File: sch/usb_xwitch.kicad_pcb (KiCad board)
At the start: 2 copper layers, 65 x 56.5 mm, 63 parts, among them J1 USB3_A, J2 USB3_A, J3 USB3_A, J4 USB3_A, J5 USB3_A, J6 USB3_A, J7 USB3_A, J8 Conn_02x05_Odd_Even, J9 C65114, K1 Relay_DPDT_Panasonic_AGQ200A4H, K2 Relay_DPDT_Panasonic_AGQ200A4H, K3 Relay_DPDT_Panasonic_AGQ200A4H, Q1 2N7002P, Q2 2N7002P, Q3 2N7002P, SW1 C2689642, U1 Pico

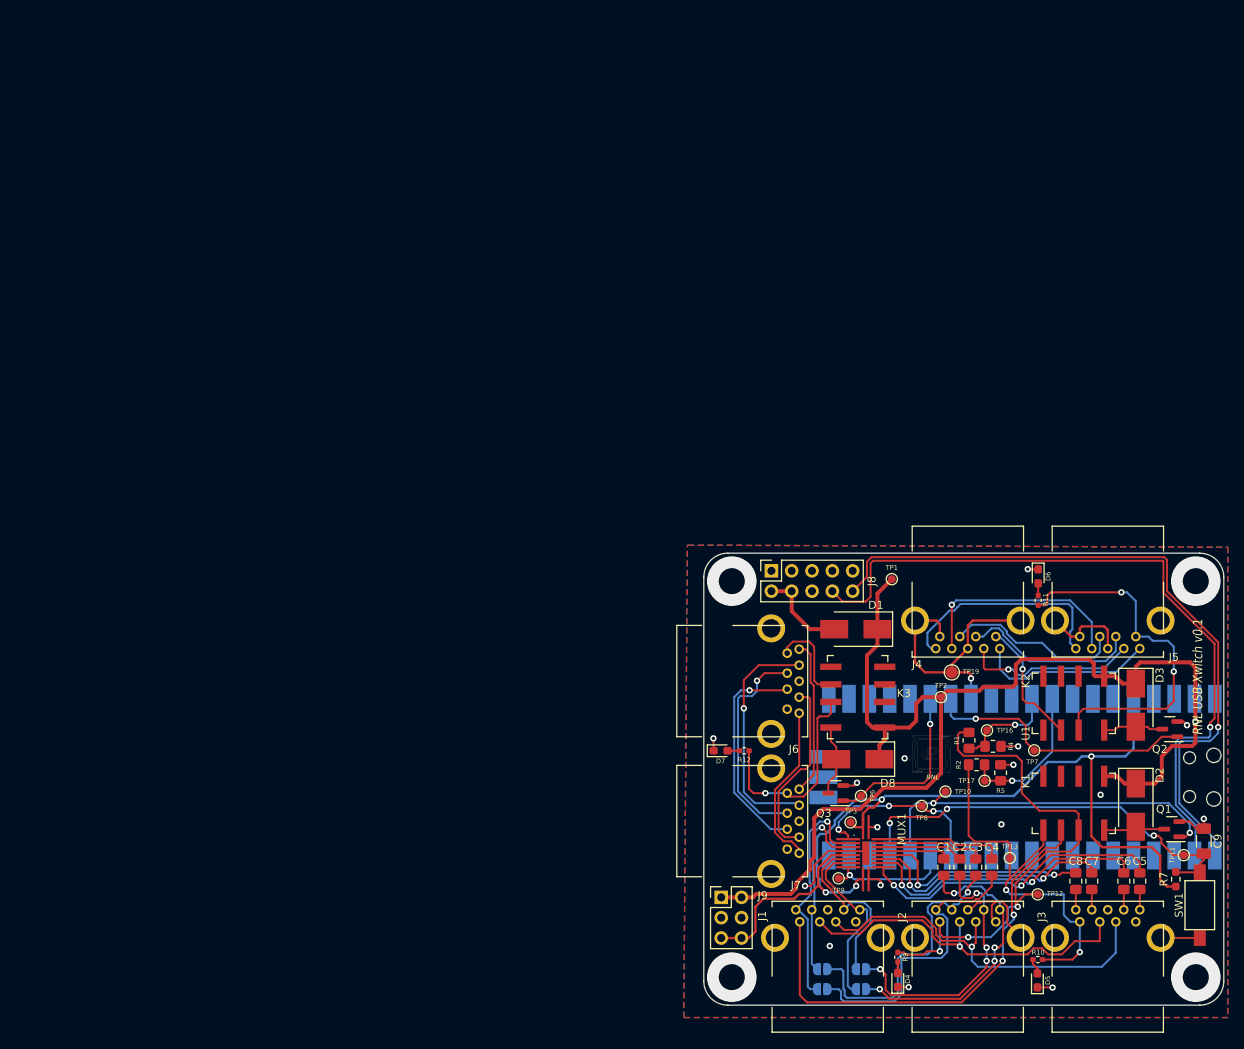
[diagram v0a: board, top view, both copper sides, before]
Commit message: updated 3d models, broken footprints, pcb re-import
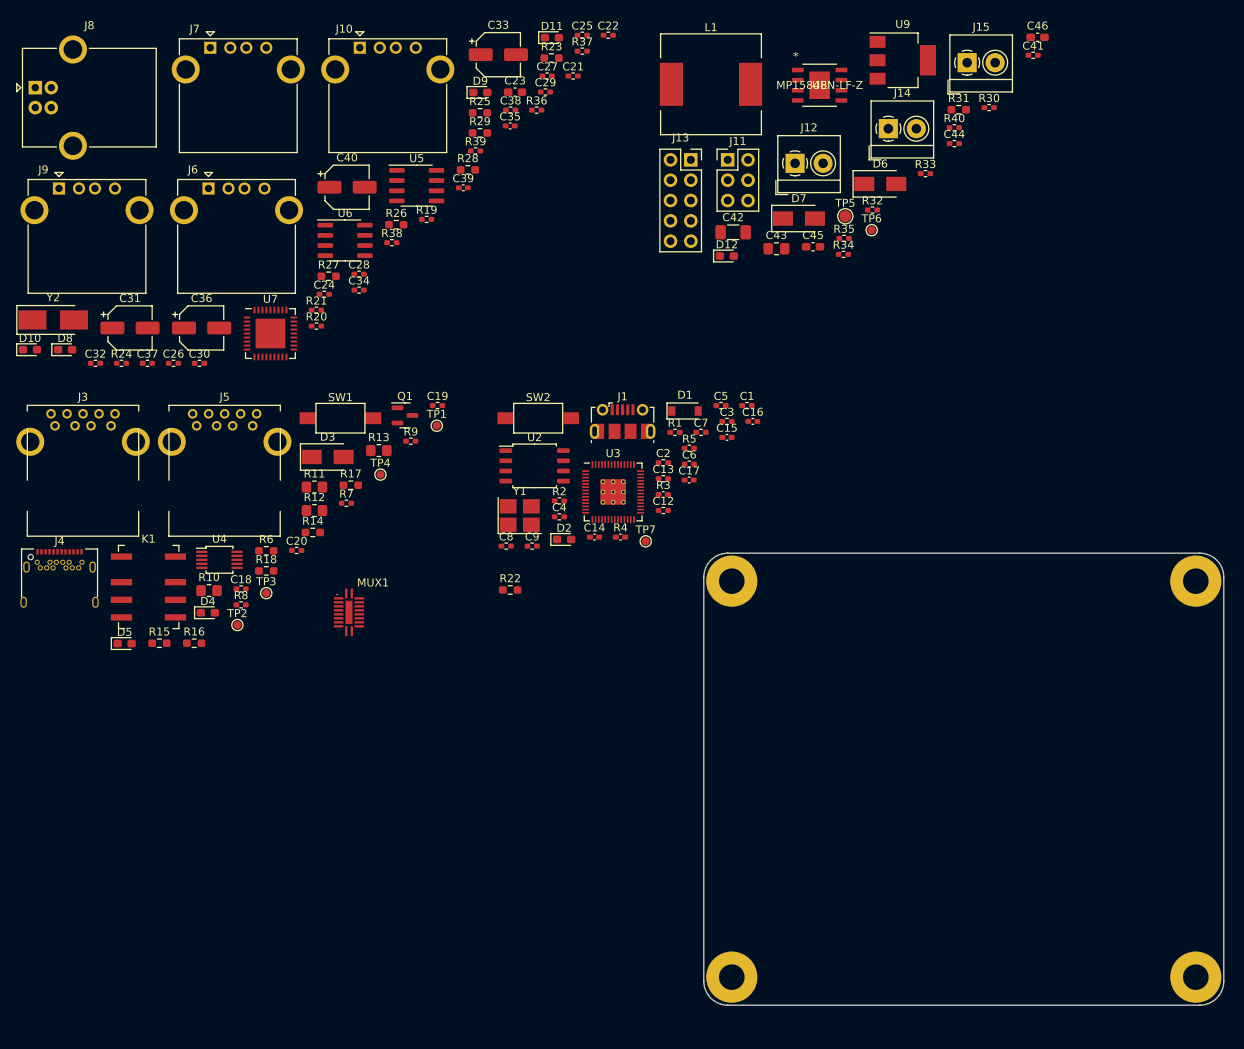
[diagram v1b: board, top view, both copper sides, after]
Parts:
- removed J2: USB3_A, usb_xwitch:USB3_A_AdamTech_USB-A3-S-RA
- removed JP1, JP2, JP3, JP4: SolderJumper_2_Open, Jumper:SolderJumper-2_P1.3mm_Open_RoundedPad1.0x1.5mm
- removed K2, K3: Relay_DPDT_Panasonic_AGQ200A4H, usb_xwitch:Relay_DPDT_Panasonic_AGQ200A4H
- removed Q2, Q3: 2N7002P, Package_TO_SOT_SMD:SOT-23
- removed RNL: LOGO, LOGO
- removed TP10, TP11, TP12, TP13, TP16, TP17, TP8, TP9: TestPoint, TestPoint:TestPoint_Pad_D1.0mm
- removed TP19: TestPoint, TestPoint:TestPoint_Pad_D1.5mm
- removed U1: Pico, usb_xwitch:RPi_Pico_SMD
- added C12: 1u, Resistor_SMD:R_0402_1005Metric_Pad0.72x0.64mm_HandSolder, F.Cu at (94.9, 74.7)
- added C13: 1u, Resistor_SMD:R_0402_1005Metric_Pad0.72x0.64mm_HandSolder, F.Cu at (94.9, 70.7)
- added C14: 2.2u, Inductor_SMD:L_0402_1005Metric_Pad0.77x0.64mm_HandSolder, F.Cu at (86.3, 78.0)
- added C15: 100n, Inductor_SMD:L_0402_1005Metric_Pad0.77x0.64mm_HandSolder, F.Cu at (102.9, 65.5)
- added C16: 30pF, Capacitor_SMD:C_0402_1005Metric_Pad0.74x0.62mm_HandSolder, F.Cu at (106.1, 63.5)
- added C17: 30pF, Capacitor_SMD:C_0402_1005Metric_Pad0.74x0.62mm_HandSolder, F.Cu at (98.2, 70.9)
- added C18: 100n, Resistor_SMD:R_0402_1005Metric_Pad0.72x0.64mm_HandSolder, F.Cu at (42.2, 84.5)
- added C19: 100n, Resistor_SMD:R_0402_1005Metric_Pad0.72x0.64mm_HandSolder, F.Cu at (66.7, 61.5)
- added C20: 100n, Resistor_SMD:R_0402_1005Metric_Pad0.72x0.64mm_HandSolder, F.Cu at (49.1, 79.7)
- added C21: 100n, Resistor_SMD:R_0402_1005Metric_Pad0.72x0.64mm_HandSolder, F.Cu at (83.7, 20.4)
- added C22: 100n, Resistor_SMD:R_0402_1005Metric_Pad0.72x0.64mm_HandSolder, F.Cu at (88.1, 15.3)
- added C23: 4.7u, Capacitor_SMD:C_0603_1608Metric_Pad1.08x0.95mm_HandSolder, F.Cu at (76.4, 22.4)
- added C24: 100n, Resistor_SMD:R_0402_1005Metric_Pad0.72x0.64mm_HandSolder, F.Cu at (52.6, 47.6)
- added C25: 100n, Resistor_SMD:R_0402_1005Metric_Pad0.72x0.64mm_HandSolder, F.Cu at (84.8, 15.3)
- added C26: 1u, Resistor_SMD:R_0402_1005Metric_Pad0.72x0.64mm_HandSolder, F.Cu at (33.7, 56.3)
- added C27: 100n, Resistor_SMD:R_0402_1005Metric_Pad0.72x0.64mm_HandSolder, F.Cu at (80.4, 20.4)
- added C28: 100n, Resistor_SMD:R_0402_1005Metric_Pad0.72x0.64mm_HandSolder, F.Cu at (56.9, 45.1)
- added C29: 100n, Resistor_SMD:R_0402_1005Metric_Pad0.72x0.64mm_HandSolder, F.Cu at (80.2, 22.4)
- added C30: 100n, Resistor_SMD:R_0402_1005Metric_Pad0.72x0.64mm_HandSolder, F.Cu at (37.0, 56.3)
- added C31: 100u, Capacitor_SMD:CP_Elec_5x5.4, F.Cu at (28.3, 51.9)
- added C32: 1u, Resistor_SMD:R_0402_1005Metric_Pad0.72x0.64mm_HandSolder, F.Cu at (24.0, 56.3)
- added C33: 100u, Capacitor_SMD:CP_Elec_5x5.4, F.Cu at (74.3, 17.7)
- added C34: 100n, Resistor_SMD:R_0402_1005Metric_Pad0.72x0.64mm_HandSolder, F.Cu at (56.9, 47.1)
- added C35: 27p, Capacitor_SMD:C_0402_1005Metric_Pad0.74x0.62mm_HandSolder, F.Cu at (75.8, 26.6)
- added C36: 100u, Capacitor_SMD:CP_Elec_5x5.4, F.Cu at (37.2, 51.9)
- added C37: 100n, Resistor_SMD:R_0402_1005Metric_Pad0.72x0.64mm_HandSolder, F.Cu at (30.5, 56.3)
- added C38: 100n, Resistor_SMD:R_0402_1005Metric_Pad0.72x0.64mm_HandSolder, F.Cu at (75.9, 24.6)
- added C39: 27p, Capacitor_SMD:C_0402_1005Metric_Pad0.74x0.62mm_HandSolder, F.Cu at (69.9, 34.3)
- added C40: 100u, Capacitor_SMD:CP_Elec_5x5.4, F.Cu at (55.4, 34.3)
- added C41: 100n, Resistor_SMD:R_0402_1005Metric_Pad0.72x0.64mm_HandSolder, F.Cu at (141.2, 17.8)
- added C42: 22u, Capacitor_SMD:C_1206_3216Metric_Pad1.33x1.80mm_HandSolder, F.Cu at (103.7, 39.9)
- added C43: 10u, Capacitor_SMD:C_0805_2012Metric_Pad1.18x1.45mm_HandSolder, F.Cu at (109.1, 42.0)
- added C44: 150pF, Resistor_SMD:R_0402_1005Metric_Pad0.72x0.64mm_HandSolder, F.Cu at (131.3, 28.8)
- added C45: 10u, Capacitor_SMD:C_0603_1608Metric_Pad1.08x0.95mm_HandSolder, F.Cu at (113.7, 41.7)
- added C46: 10u, Capacitor_SMD:C_0603_1608Metric_Pad1.08x0.95mm_HandSolder, F.Cu at (141.7, 15.5)
- added D10: 19-217/GHC-YR1S2/3T, Diode_SMD:D_0603_1608Metric_Pad1.05x0.95mm_HandSolder, F.Cu at (15.8, 54.6)
- added D11: 19-217/GHC-YR1S2/3T, Diode_SMD:D_0603_1608Metric_Pad1.05x0.95mm_HandSolder, F.Cu at (81.0, 15.6)
- added D12: 19-217/GHC-YR1S2/3T, Diode_SMD:D_0603_1608Metric_Pad1.05x0.95mm_HandSolder, F.Cu at (102.9, 42.9)
- added D9: 19-217/GHC-YR1S2/3T, Diode_SMD:D_0603_1608Metric_Pad1.05x0.95mm_HandSolder, F.Cu at (72.1, 22.4)
- added H1: RPI Mounting Hole, MountingHole:MountingHole_3.2mm_M3_Pad, F.Cu at (103.5, 83.5)
- added H2: RPI Mounting Hole, MountingHole:MountingHole_3.2mm_M3_Pad, F.Cu at (161.5, 83.5)
- added H3: RPI Mounting Hole, MountingHole:MountingHole_3.2mm_M3_Pad, F.Cu at (161.5, 133.0)
- added H4: RPI Mounting Hole, MountingHole:MountingHole_3.2mm_M3_Pad, F.Cu at (103.5, 133.0)
- added J10: USB_A, Connector_USB:USB_A_CONNFLY_DS1095-WNR0, F.Cu at (57.0, 16.8)
- added J11: C65114, Connector_PinHeader_2.54mm:PinHeader_2x03_P2.54mm_Vertical, F.Cu at (103.0, 30.8)
- added J12: Screw_Terminal_3.5mm, TerminalBlock_4Ucon:TerminalBlock_4Ucon_1x02_P3.50mm_Horizontal, F.Cu at (111.4, 31.3)
- added J13: Conn_02x05_Odd_Even, Connector_PinSocket_2.54mm:PinSocket_2x05_P2.54mm_Vertical, F.Cu at (98.4, 30.8)
- added J14: Screw_Terminal_3.5mm, TerminalBlock_4Ucon:TerminalBlock_4Ucon_1x02_P3.50mm_Horizontal, F.Cu at (123.1, 26.9)
- added J15: Screw_Terminal_3.5mm, TerminalBlock_4Ucon:TerminalBlock_4Ucon_1x02_P3.50mm_Horizontal, F.Cu at (132.9, 18.7)
- added L1: 15u, Inductor_SMD:L_12x12mm_H6mm, F.Cu at (100.9, 21.4)
- added R13: 33K, Resistor_SMD:R_0805_2012Metric_Pad1.20x1.40mm_HandSolder, F.Cu at (59.4, 67.2)
- added R14: 0R, Resistor_SMD:R_0603_1608Metric_Pad0.98x0.95mm_HandSolder, F.Cu at (51.1, 77.4)
- added R15: 0R, Resistor_SMD:R_0603_1608Metric_Pad0.98x0.95mm_HandSolder, F.Cu at (31.9, 91.3)
- added R16: 0R, Resistor_SMD:R_0603_1608Metric_Pad0.98x0.95mm_HandSolder, F.Cu at (36.3, 91.3)
- added R17: 0R, Resistor_SMD:R_0603_1608Metric_Pad0.98x0.95mm_HandSolder, F.Cu at (55.9, 71.5)
- added R18: 0R, Resistor_SMD:R_0603_1608Metric_Pad0.98x0.95mm_HandSolder, F.Cu at (45.3, 82.2)
- added R19: 100K, Resistor_SMD:R_0402_1005Metric_Pad0.72x0.64mm_HandSolder, F.Cu at (65.4, 38.3)
- added R20: 100K, Resistor_SMD:R_0402_1005Metric_Pad0.72x0.64mm_HandSolder, F.Cu at (51.6, 51.6)
- added R21: 100K, Resistor_SMD:R_0402_1005Metric_Pad0.72x0.64mm_HandSolder, F.Cu at (51.6, 49.6)
- added R22: 12K, Resistor_SMD:R_0603_1608Metric_Pad0.98x0.95mm_HandSolder, F.Cu at (75.8, 84.6)
- added R23: 1M, Resistor_SMD:R_0603_1608Metric_Pad0.98x0.95mm_HandSolder, F.Cu at (81.0, 18.1)
- added R24: 100K, Resistor_SMD:R_0402_1005Metric_Pad0.72x0.64mm_HandSolder, F.Cu at (27.2, 56.3)
- added R25: 10K, Resistor_SMD:R_0603_1608Metric_Pad0.98x0.95mm_HandSolder, F.Cu at (72.0, 25.0)
- added R26: 10K, Resistor_SMD:R_0603_1608Metric_Pad0.98x0.95mm_HandSolder, F.Cu at (61.6, 38.9)
- added R27: 100K, Resistor_SMD:R_0603_1608Metric_Pad0.98x0.95mm_HandSolder, F.Cu at (53.1, 45.4)
- added R28: 100K, Resistor_SMD:R_0603_1608Metric_Pad0.98x0.95mm_HandSolder, F.Cu at (70.5, 32.1)
- added R29: 10K, Resistor_SMD:R_0603_1608Metric_Pad0.98x0.95mm_HandSolder, F.Cu at (72.0, 27.5)
- added R3: 1K, Inductor_SMD:L_0402_1005Metric_Pad0.77x0.64mm_HandSolder, F.Cu at (94.9, 72.7)
- added R30: 100K, Resistor_SMD:R_0402_1005Metric_Pad0.72x0.64mm_HandSolder, F.Cu at (135.7, 24.3)
- added R31: 24.9k, Resistor_SMD:R_0603_1608Metric_Pad0.98x0.95mm_HandSolder, F.Cu at (131.9, 24.6)
- added R32: 210k, Resistor_SMD:R_0402_1005Metric_Pad0.72x0.64mm_HandSolder, F.Cu at (121.1, 37.1)
- added R33: 100K, Resistor_SMD:R_0402_1005Metric_Pad0.72x0.64mm_HandSolder, F.Cu at (127.7, 32.6)
- added R34: 40.2K, Resistor_SMD:R_0402_1005Metric_Pad0.72x0.64mm_HandSolder, F.Cu at (117.5, 42.6)
- added R35: 100K, Resistor_SMD:R_0402_1005Metric_Pad0.72x0.64mm_HandSolder, F.Cu at (117.5, 40.7)
- added R36: 330, Resistor_SMD:R_0402_1005Metric_Pad0.72x0.64mm_HandSolder, F.Cu at (79.1, 24.6)
- added R37: 330, Resistor_SMD:R_0402_1005Metric_Pad0.72x0.64mm_HandSolder, F.Cu at (84.8, 17.2)
- added R38: 330, Resistor_SMD:R_0402_1005Metric_Pad0.72x0.64mm_HandSolder, F.Cu at (61.0, 41.2)
- added R39: 330, Resistor_SMD:R_0402_1005Metric_Pad0.72x0.64mm_HandSolder, F.Cu at (71.5, 29.7)
- added R40: 510, Resistor_SMD:R_0402_1005Metric_Pad0.72x0.64mm_HandSolder, F.Cu at (131.3, 26.8)
- added R6: 10K, Resistor_SMD:R_0603_1608Metric_Pad0.98x0.95mm_HandSolder, F.Cu at (45.3, 79.7)
- added R8: 330, Resistor_SMD:R_0402_1005Metric_Pad0.72x0.64mm_HandSolder, F.Cu at (42.2, 86.5)
- added SW2: C2689642, usb_xwitch:SW_SPST_CK_PTS636_SP43_SMTR, F.Cu at (79.3, 63.1)
- added TP4: TestPoint, TestPoint:TestPoint_Pad_D1.0mm, F.Cu at (59.6, 70.2)
- added TP5: TestPoint, TestPoint:TestPoint_Pad_D1.5mm, F.Cu at (117.7, 37.9)
- added U2: W25Q64JVSSIQ, Package_SO:SOIC-8_5.23x5.23mm_P1.27mm, F.Cu at (78.8, 69.1)
- added U3: RP2040, usb_xwitch:RP2040-QFN-56, F.Cu at (88.7, 72.3)
- added U4: FSUSB42MUX, Package_SO:MSOP-10_3x3mm_P0.5mm, F.Cu at (39.5, 80.8)
- added U5: MIC2026-1BM, Package_SO:SOIC-8_3.9x4.9mm_P1.27mm, F.Cu at (64.1, 34.1)
- added U6: MIC2026-1BM, Package_SO:SOIC-8_3.9x4.9mm_P1.27mm, F.Cu at (55.2, 40.9)
- added U7: USB2514B_Bi, Package_DFN_QFN:QFN-36-1EP_6x6mm_P0.5mm_EP3.7x3.7mm, F.Cu at (45.8, 52.5)
- added U8: MP1584EN-LF-Z, usb_xwitch:MP1584EN-LF-Z, F.Cu at (114.5, 21.5)
- added U9: NCP1117LPST33T3G, Package_TO_SOT_SMD:SOT-223-3_TabPin2, F.Cu at (124.9, 18.4)
- added Y1: 12MHz, Crystal:Crystal_SMD_3225-4Pin_3.2x2.5mm_HandSoldering, F.Cu at (77.0, 75.3)
- added Y2: 24MHz, Crystal:Crystal_SMD_5032-2Pin_5.0x3.2mm_HandSoldering, F.Cu at (18.7, 50.9)
- C1, C2, C3, C4, C5, C6, C7, C8: footprint Capacitor_SMD:C_0805_2012Metric_Pad1.18x1.45mm_HandSolder -> Resistor_SMD:R_0402_1005Metric_Pad0.72x0.64mm_HandSolder
- C9: footprint Capacitor_SMD:C_1206_3216Metric_Pad1.33x1.80mm_HandSolder -> Resistor_SMD:R_0402_1005Metric_Pad0.72x0.64mm_HandSolder
- D1: value VS-10BQ015 -> B5819W SL; footprint Diode_SMD:D_SMB_Handsoldering -> Diode_SMD:D_SOD-123
- D2, D8: value VS-10BQ015 -> 19-217/GHC-YR1S2/3T; footprint Diode_SMD:D_SMB_Handsoldering -> Diode_SMD:D_0603_1608Metric_Pad1.05x0.95mm_HandSolder
- D3: value VS-10BQ015 -> SS34; footprint Diode_SMD:D_SMB_Handsoldering -> Diode_SMD:D_SMA
- D6, D7: value 19-217/GHC-YR1S2/3T -> SS34; footprint Diode_SMD:D_0603_1608Metric_Pad1.05x0.95mm_HandSolder -> Diode_SMD:D_SMA
- J1: value USB3_A -> USB_B_Micro; footprint usb_xwitch:USB3_A_AdamTech_USB-A3-S-RA -> Connector_USB:USB_Micro-B_Molex-105017-0001
- J4: value USB3_A -> USB_C_Receptacle; footprint usb_xwitch:USB3_A_AdamTech_USB-A3-S-RA -> usb_xwitch:USB_TypeC_24Pin_ShouHan
- J6, J7: value USB3_A -> USB_A; footprint usb_xwitch:USB3_A_AdamTech_USB-A3-S-RA -> Connector_USB:USB_A_CONNFLY_DS1095-WNR0
- J8: value Conn_02x05_Odd_Even -> USB_B; footprint Connector_PinSocket_2.54mm:PinSocket_2x05_P2.54mm_Vertical -> Connector_USB:USB_B_OST_USB-B1HSxx_Horizontal
- J9: value C65114 -> USB_A; footprint Connector_PinHeader_2.54mm:PinHeader_2x03_P2.54mm_Vertical -> Connector_USB:USB_A_CONNFLY_DS1095-WNR0
- R1, R2: value 18K -> 27.4R; footprint Resistor_SMD:R_0805_2012Metric_Pad1.20x1.40mm_HandSolder -> Resistor_SMD:R_0402_1005Metric_Pad0.72x0.64mm_HandSolder
- R10, R11: value 330Ω -> 18K; footprint Resistor_SMD:R_0402_1005Metric_Pad0.72x0.64mm_HandSolder -> Resistor_SMD:R_0805_2012Metric_Pad1.20x1.40mm_HandSolder
- R12: value 330Ω -> 33K; footprint Resistor_SMD:R_0402_1005Metric_Pad0.72x0.64mm_HandSolder -> Resistor_SMD:R_0805_2012Metric_Pad1.20x1.40mm_HandSolder
- R4: value 33K -> 1K; footprint Resistor_SMD:R_0805_2012Metric_Pad1.20x1.40mm_HandSolder -> Inductor_SMD:L_0402_1005Metric_Pad0.77x0.64mm_HandSolder
- R5: value 33K -> 470R; footprint Resistor_SMD:R_0805_2012Metric_Pad1.20x1.40mm_HandSolder -> Resistor_SMD:R_0402_1005Metric_Pad0.72x0.64mm_HandSolder
- R7: value 10K -> 330; footprint Resistor_SMD:R_0603_1608Metric_Pad0.98x0.95mm_HandSolder -> Resistor_SMD:R_0402_1005Metric_Pad0.72x0.64mm_HandSolder
- R9: value 330Ω -> 56K
- moved J3 142.3 mm to (18.9, 64.1)
- moved SW1 123.5 mm to (54.6, 63.1), turned to 0 degrees
- moved D5 121.6 mm to (27.6, 91.3), turned to 0 degrees
- moved J9 121.3 mm to (19.4, 34.4)
- moved J5 120.3 mm to (36.6, 64.1), turned to 0 degrees
- moved K1 118.8 mm to (30.6, 84.2), turned to 0 degrees
- moved J7 117.8 mm to (38.3, 16.8), turned to 0 degrees
- moved J4 117.2 mm to (19.5, 84.8), turned to 0 degrees
- moved R7 113.8 mm to (55.3, 73.8), turned to 0 degrees
- moved R10 113.4 mm to (38.2, 84.7), turned to 0 degrees
- moved D8 111.5 mm to (20.2, 54.6), turned to 0 degrees
- moved J8 110.1 mm to (16.4, 21.8), turned to 0 degrees
- moved Q1 108.9 mm to (62.6, 62.8), turned to 0 degrees
- moved D3 105.7 mm to (53.0, 68.0), turned to 0 degrees
- moved D4 97.7 mm to (38.0, 87.5), turned to 0 degrees
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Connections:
- C1 pad 1: Net-(C1-Pad1) -> +1V1
- C1 pad 2: /RX-BP1 -> GND
- C2 pad 1: Net-(C2-Pad1) -> +1V1
- C2 pad 2: /RX+BP1 -> GND
- C3 pad 1: Net-(C3-Pad1) -> +3V3
- C3 pad 2: /TX-BP1 -> GND
- C4 pad 1: Net-(C4-Pad1) -> +3V3
- C4 pad 2: /TX+BP1 -> GND
- C5 pad 1: Net-(C5-Pad1) -> +3V3
- C5 pad 2: Net-(C5-Pad2) -> GND
- C6 pad 1: Net-(C6-Pad1) -> +3V3
- C6 pad 2: Net-(C6-Pad2) -> GND
- C7 pad 1: Net-(C7-Pad1) -> +3V3
- C7 pad 2: Net-(C7-Pad2) -> GND
- C8 pad 1: Net-(C8-Pad1) -> +3V3
- C8 pad 2: Net-(C8-Pad2) -> GND
- C9 pad 1: GND -> +3V3
- C9 pad 2: /SW-A -> GND
- D2 pad 1: +5V -> GND
- D2 pad 2: /RL1 -> Net-(D2-Pad2)
- D3 pad 2: /RL2 -> /usb3_switch/RL1
- D6 pad 1: GND -> Net-(C41-Pad1)
- D6 pad 2: Net-(D6-Pad2) -> GND
- D7 pad 1: GND -> +5V
- D8 pad 1: +5V -> GND
- D8 pad 2: /RL3 -> Net-(D8-Pad2)
- J1 pad 1: Net-(J1-Pad1) -> Net-(D1-Pad2)
- J1 pad 2: Net-(J1-Pad2) -> /xwitch_controller/USB_D-
- J1 pad 3: Net-(J1-Pad3) -> /xwitch_controller/USB_D+
- J1 pad 4: GND -> unconnected-(J1-Pad4)
- J1 pad 5: /RX-BP -> GND
- J1 pad 6: /RX+BP -> GND
- J3 pad 1: /VBUS_1_2 -> /usb3_switch/VBUS_1_1
- J3 pad 10: GND -> Net-(J3-Pad10)
- J3 pad 2: Net-(J1-Pad2) -> Net-(J3-Pad2)
- J3 pad 3: Net-(J1-Pad3) -> Net-(J3-Pad3)
- J3 pad 4: GND -> Net-(J3-Pad4)
- J3 pad 5: Net-(C5-Pad2) -> Net-(J3-Pad5)
- J3 pad 6: Net-(C6-Pad2) -> Net-(J3-Pad6)
- J3 pad 7: GND -> Net-(J3-Pad4)
- J3 pad 8: Net-(C7-Pad2) -> Net-(J3-Pad8)
- J3 pad 9: Net-(C8-Pad2) -> Net-(J3-Pad9)
- J5 pad 1: /VBUS2 -> /usb3_switch/VBUS_1_2
- J5 pad 10: GND -> Net-(J5-Pad10)
- J5 pad 2: Net-(J4-Pad2) -> Net-(J5-Pad2)
- J5 pad 3: Net-(J4-Pad3) -> Net-(J5-Pad3)
- J5 pad 4: GND -> Net-(J5-Pad4)
- J5 pad 5: Net-(J4-Pad5) -> Net-(J5-Pad5)
- J5 pad 6: Net-(J4-Pad6) -> Net-(J5-Pad6)
- J5 pad 7: GND -> Net-(J5-Pad4)
- J5 pad 8: Net-(J4-Pad8) -> Net-(J5-Pad8)
- J5 pad 9: Net-(J4-Pad9) -> Net-(J5-Pad9)
- J6 pad 1: Net-(J6-Pad1) -> /usb2_hub/V_Ch1
- J6 pad 5: Net-(J6-Pad5) -> GND
- J7 pad 1: /VBUS3 -> /usb2_hub/V_Ch2
- J7 pad 2: Net-(J6-Pad2) -> Net-(J7-Pad2)
- J7 pad 3: Net-(J6-Pad3) -> Net-(J7-Pad3)
- J7 pad 5: Net-(J6-Pad5) -> GND
- J8 pad 1: unconnected-(J8-Pad1) -> Net-(C32-Pad1)
- J8 pad 2: Net-(D1-Pad2) -> Net-(J8-Pad2)
- J8 pad 3: unconnected-(J8-Pad3) -> Net-(J8-Pad3)
- J8 pad 4: Net-(D1-Pad2) -> GND
- J8 pad 5: unconnected-(J8-Pad5) -> GND
- J9 pad 1: +5V -> /usb2_hub/V_Ch3
- J9 pad 2: +5V -> Net-(J9-Pad2)
- J9 pad 3: GND -> Net-(J9-Pad3)
- J9 pad 5: +3V3 -> GND
- K1 pad 2: unconnected-(K1-Pad2) -> Net-(J3-Pad4)
- K1 pad 3: unconnected-(K1-Pad3) -> GND
- K1 pad 4: unconnected-(K1-Pad4) -> Net-(J5-Pad4)
- K1 pad 5: /VBUS_1_2 -> /usb3_switch/VBUS_1_2
- K1 pad 6: Net-(J1-Pad1) -> Net-(J4-PadA4)
- K1 pad 7: /VBUS_1_1 -> /usb3_switch/VBUS_1_1
- K1 pad 8: /RL1 -> /usb3_switch/RL1
- MUX1 pad 12: Net-(C5-Pad1) -> Net-(J5-Pad8)
- MUX1 pad 13: Net-(C6-Pad1) -> Net-(J5-Pad9)
- MUX1 pad 14: Net-(C7-Pad1) -> Net-(J5-Pad5)
- MUX1 pad 15: Net-(C8-Pad1) -> Net-(J5-Pad6)
- MUX1 pad 16: Net-(C1-Pad1) -> Net-(J3-Pad8)
- MUX1 pad 17: Net-(C2-Pad1) -> Net-(J3-Pad9)
- MUX1 pad 18: Net-(C3-Pad1) -> Net-(J3-Pad5)
- MUX1 pad 19: Net-(C4-Pad1) -> Net-(J3-Pad6)
- MUX1 pad 2: /PD-A -> /usb3_switch/PD-SU3
- MUX1 pad 3: /TX+BP -> Net-(J4-PadA2)
- MUX1 pad 4: /TX-BP -> Net-(J4-PadA3)
- MUX1 pad 7: /RX+BP -> Net-(J4-PadB11)
- MUX1 pad 8: /RX-BP -> Net-(J4-PadB10)
- MUX1 pad 9: /SEL-A -> /usb3_switch/SEL-SU3
- Q1 pad 1: /REL-A -> /usb3_switch/REL-CTL
- Q1 pad 3: /RL1 -> /usb3_switch/RL1
- R1 pad 1: /VBUS_1_1 -> Net-(R1-Pad1)
- R1 pad 2: /V_1_1 -> /xwitch_controller/USB_D+
- R10 pad 1: /VBUS_1_2 -> /usb3_switch/VBUS_1_1
- R10 pad 2: Net-(D5-Pad2) -> /usb3_switch/V_1_1
- R11 pad 1: /VBUS2 -> /usb3_switch/VBUS_1_2
- R11 pad 2: Net-(D6-Pad2) -> /usb3_switch/V_1_2
- R12 pad 1: /VBUS3 -> /usb3_switch/V_1_1
- R12 pad 2: Net-(D7-Pad2) -> GND
- R2 pad 1: /VBUS_1_2 -> Net-(R2-Pad1)
- R2 pad 2: /V_1_2 -> /xwitch_controller/USB_D-
- R4 pad 1: /V_1_1 -> /xwitch_controller/XOUT
- R4 pad 2: GND -> Net-(C17-Pad1)
- R5 pad 1: /V_1_2 -> /xwitch_controller/GPIO25_LED
- R5 pad 2: GND -> Net-(D2-Pad2)
- R7 pad 1: +3V3 -> /usb3_switch/VBUS_1_1
- R7 pad 2: /SW-A -> Net-(D4-Pad2)
- R9 pad 1: /VBUS_1_1 -> Net-(J4-PadA4)
- R9 pad 2: Net-(D4-Pad2) -> Net-(J4-PadA5)
- SW1 pad 2: /SW-A -> /usb3_switch/SW-INTR
- TP1 pad 1: +5V -> /usb3_switch/VBUS_1_1
- TP2 pad 1: +5V -> /usb3_switch/VBUS_1_2
- TP3 pad 1: +3V3 -> /usb3_switch/V_1_1
- TP6 pad 1: /REL-C -> +5V
- TP7 pad 1: /REL-B -> +1V1
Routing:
- net +5V: track 149.6 -> 0.00 mm, vias 1 -> 0
- net +3V3: track 118.8 -> 0.00 mm, vias 4 -> 0
- net GND: track 96.2 -> 0.00 mm, vias 17 -> 0
- net /UART_PI_TX: track 90.2 -> 0.00 mm, vias 1 -> 0
- net /UART_PI_RX: track 86.9 -> 0.00 mm, vias 1 -> 0
- net /VBUS_1_1: track 67.2 -> 0.00 mm, vias 3 -> 0
- net Net-(J1-Pad1): track 57.4 -> 0.00 mm, vias 2 -> 0
- net /SW-A: track 52.0 -> 0.00 mm, vias 3 -> 0
- net /VBUS_1_2: track 49.4 -> 0.00 mm, vias 2 -> 0
- net Net-(J1-Pad3): track 48.1 -> 0.00 mm, vias 1 -> 0
- net /REL-A: track 45.9 -> 0.00 mm, vias 2 -> 0
- net Net-(J1-Pad2): track 45.3 -> 0.00 mm, vias 1 -> 0
- net /VBUS2: track 45.0 -> 0.00 mm, vias 2 -> 0
- net Net-(C5-Pad1): track 38.7 -> 0.00 mm, vias 2 -> 0
- net /RX-BP1: track 37.4 -> 0.00 mm, vias 4 -> 0
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- removed copper zone on B.Cu, net GND
- removed copper zone on F.Cu, net GND
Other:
- board text removed: "JLCJLCJLCJLC"
- board text removed: "RNL USB-Xwitch v0.1"

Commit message: fix sch unexpect to gnd; usb to right angle; pcb boarder increased to pi size
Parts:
- J10, J6, J7, J9: footprint Connector_USB:USB_A_CONNFLY_DS1095-WNR0 -> Connector_USB:USB_A_Wuerth_614004134726_Horizontal
- moved C23 181.1 mm to (257.5, 27.9)
- moved C21 181.1 mm to (264.7, 25.9)
- moved C22 181.1 mm to (269.1, 20.8)
- moved C24 181.1 mm to (233.6, 53.2)
- moved C25 181.1 mm to (265.9, 20.8)
- moved C26 181.1 mm to (214.8, 61.8)
- moved C27 181.1 mm to (261.5, 25.9)
- moved C28 181.1 mm to (238.0, 50.7)
- moved C29 181.1 mm to (261.3, 27.9)
- moved C30 181.1 mm to (218.0, 61.8)
- moved C31 181.1 mm to (209.3, 57.4)
- moved C32 181.1 mm to (205.0, 61.8)
- moved C33 181.1 mm to (255.4, 23.2)
- moved C34 181.1 mm to (238.0, 52.7)
- moved C35 181.1 mm to (256.9, 32.1)
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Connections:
- C43 pad 1: GND -> Net-(C43-Pad1)
- J12 pad 1: GND -> Net-(C43-Pad1)
- R30 pad 2: GND -> Net-(C43-Pad1)
- U8 pad 7: GND -> Net-(C43-Pad1)
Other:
- board size 65 x 56.5 mm -> 84 x 56.5 mm
- copper layers 2 -> 4

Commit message: correct usb footprints
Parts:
- removed J11: C65114, Connector_PinHeader_2.54mm:PinHeader_2x03_P2.54mm_Vertical
- removed TP5: TestPoint, TestPoint:TestPoint_Pad_D1.5mm
- added Q2: 2N7002P, Package_TO_SOT_SMD:SOT-23, F.Cu at (156.2, 47.5)
- C34: value 100n -> DNP
- moved R36 100.0 mm to (177.6, 86.5)
- moved J14 68.4 mm to (149.8, 134.4), turned to 0 degrees
- moved U8 63.9 mm to (106.4, 106.7), turned to -90 degrees
- moved C43 58.9 mm to (110.2, 114.5)
- moved D8 33.4 mm to (181.1, 86.7), turned to 180 degrees
- moved J15 19.1 mm to (170.3, 134.4)
- moved L1 6.65 mm to (117.0, 105.9)
- moved J1 0.07 mm to (136.5, 82.7)
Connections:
- U3 pad 29: /xwitch_controller/GPIO18 -> /usb2_hub/RST_CTL
- U7 pad 30: Net-(J8-Pad3) -> Net-(J8-Pad2)
- U7 pad 31: Net-(J8-Pad2) -> Net-(J8-Pad3)

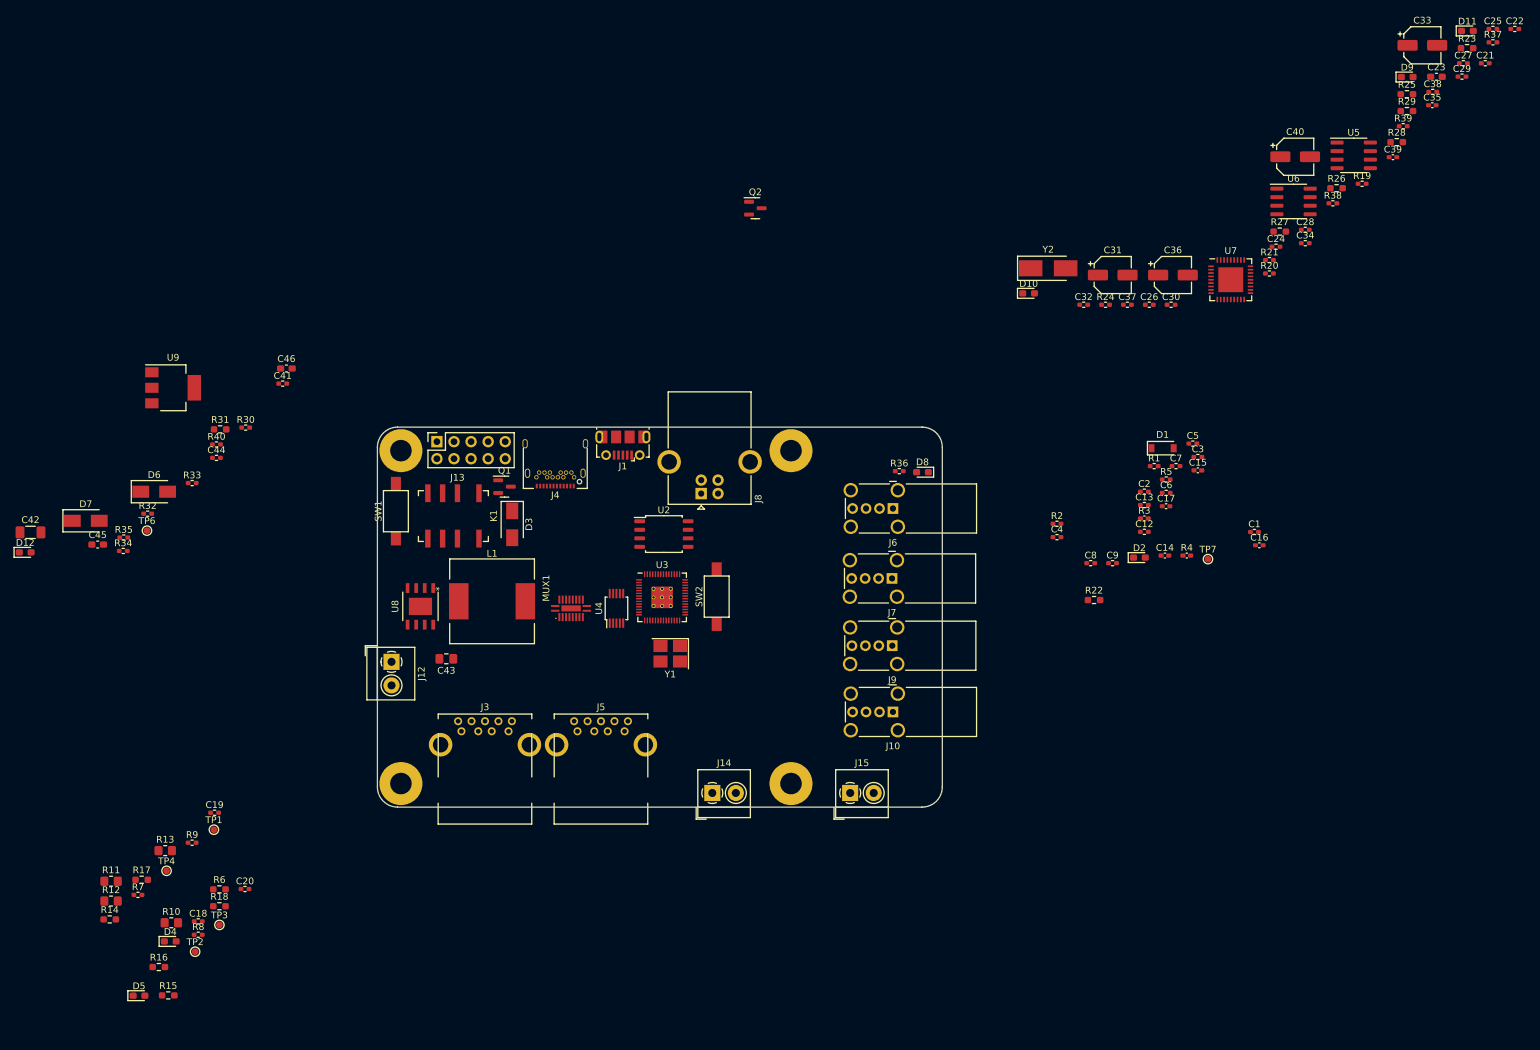
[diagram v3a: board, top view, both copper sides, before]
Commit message: pcb layout update and some res package changed
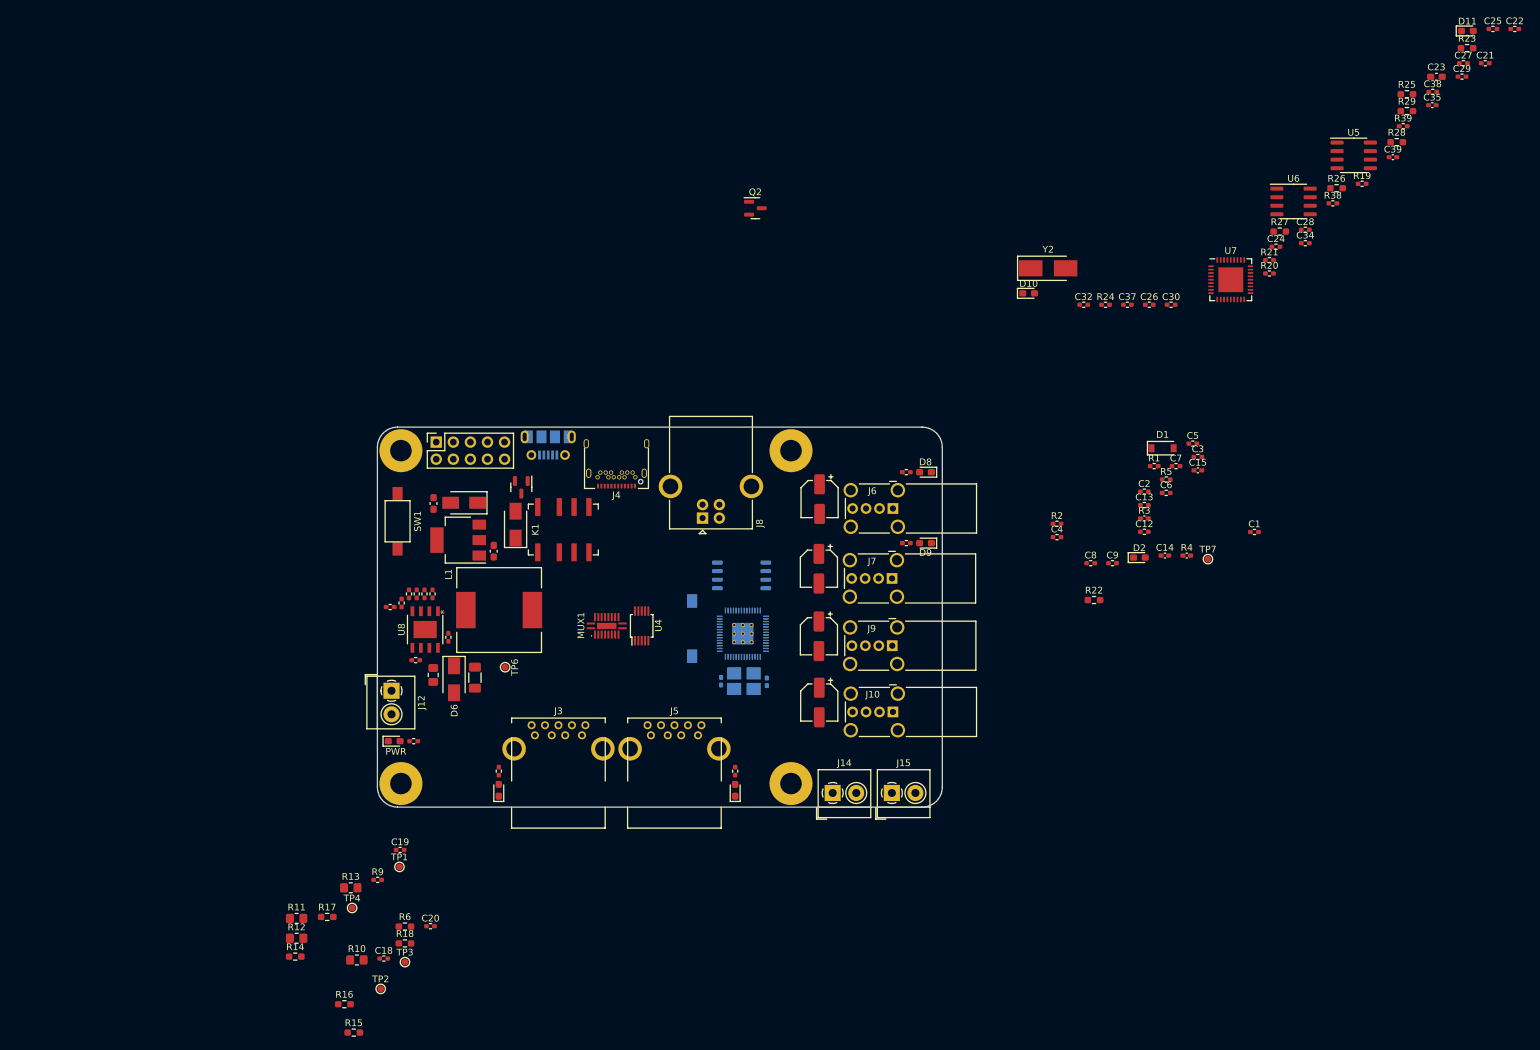
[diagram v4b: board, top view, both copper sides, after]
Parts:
- C16, C17, J1, SW2, U2, U3, Y1: moved to B.Cu
- R31: footprint Resistor_SMD:R_0603_1608Metric_Pad0.98x0.95mm_HandSolder -> Resistor_SMD:R_0402_1005Metric_Pad0.72x0.64mm_HandSolder
- moved C33 118.8 mm to (165.7, 101.0), turned to -90 degrees
- moved R37 114.7 mm to (178.7, 97.2)
- moved C40 107.7 mm to (165.7, 121.0), turned to -90 degrees
- moved D9 99.7 mm to (181.5, 97.2), turned to 180 degrees
- moved D5 93.8 mm to (153.2, 134.0), turned to 90 degrees
- moved R8 83.5 mm to (153.2, 131.2), turned to -90 degrees
- moved C16 82.6 mm to (151.1, 117.8), turned to -90 degrees
- moved C36 75.2 mm to (165.7, 111.1), turned to -90 degrees
- moved C42 69.5 mm to (114.5, 117.2), turned to -90 degrees
- moved C17 64.9 mm to (157.9, 117.9), turned to 90 degrees
- moved D12 61.6 mm to (102.5, 126.7)
- moved C45 58.9 mm to (117.3, 98.5), turned to -90 degrees
- moved TP6 57.0 mm to (119.0, 115.7), turned to -90 degrees
- moved R7 56.7 mm to (118.0, 131.2), turned to 90 degrees
- moved D7 56.3 mm to (112.9, 91.2), turned to 180 degrees
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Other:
- board text added: "PWR"

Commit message: update pcb
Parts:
- moved U7 89.5 mm to (154.0, 110.0)
- moved Y2 64.8 mm to (154.4, 102.7)
- moved C17 31.6 mm to (126.3, 116.7)
- moved SW2 31.6 mm to (115.2, 108.8)
- moved U2 31.6 mm to (122.6, 100.9)
- moved U3 31.6 mm to (122.8, 109.6)
- moved C16 31.6 mm to (119.5, 116.6)
- moved Y1 31.6 mm to (123.0, 116.6)
- moved J3 17.3 mm to (140.7, 125.8)
- moved J5 17.3 mm to (123.4, 125.8)
- turned MUX1 to -90 degrees

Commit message: pcb layout update
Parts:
- R10, R11, R12, R13, TP1, TP2, TP3, TP4: moved to B.Cu
- moved U5 115.5 mm to (159.2, 116.8), turned to 90 degrees
- moved U6 90.2 mm to (161.8, 97.5), turned to 90 degrees
- moved R16 86.8 mm to (139.7, 91.4), turned to 90 degrees
- moved TP2 75.7 mm to (134.3, 95.8), turned to 180 degrees
- moved R12 73.2 mm to (138.2, 102.8), turned to -90 degrees
- moved R10 73.2 mm to (138.2, 98.8), turned to -90 degrees
- moved R14 73.1 mm to (153.7, 126.9), turned to 90 degrees
- moved R15 72.9 mm to (155.2, 126.9), turned to -90 degrees
- moved R11 71.3 mm to (134.3, 98.8), turned to -90 degrees
- moved C18 70.3 mm to (106.8, 89.0)
- moved TP3 68.4 mm to (140.7, 101.8), turned to 180 degrees
- moved R9 65.1 mm to (129.2, 89.1), turned to 90 degrees
- moved R6 62.9 mm to (106.2, 91.3), turned to 90 degrees
- moved TP1 60.7 mm to (138.2, 95.8), turned to 180 degrees
- moved TP4 60.5 mm to (130.8, 101.8), turned to 180 degrees
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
